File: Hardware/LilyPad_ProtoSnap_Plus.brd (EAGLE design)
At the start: 109.2 x 82.5 mm, 197 parts, among them J1 SEWTAP_LONG-2SIDE, J10 SEWTAP_LONG-2SIDE, J11 SEWTAP_LONG-2SIDE, J12 SEWTAP_LONG-2SIDE, J13 SEWTAP_LONG-2SIDE, J14 SEWTAP_LONG-2SIDE, J15 AMP FCI 10103594-0001LF, J2 SEWTAP_LONG-2SIDE, J3 SEWTAP_LONG-2SIDE, J4 SEWTAP_LONG-2SIDE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

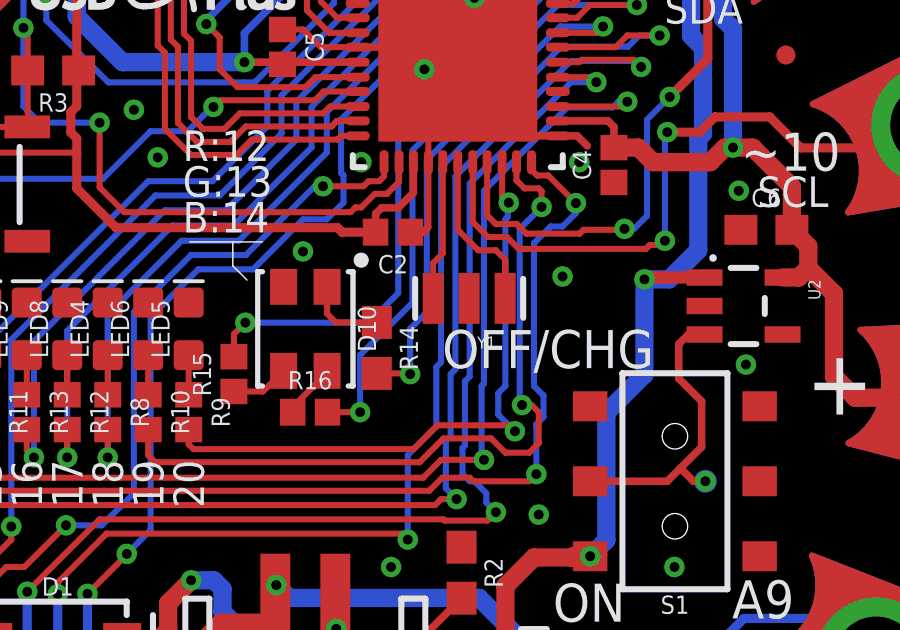
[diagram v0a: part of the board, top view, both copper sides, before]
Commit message: Added changes from reds review
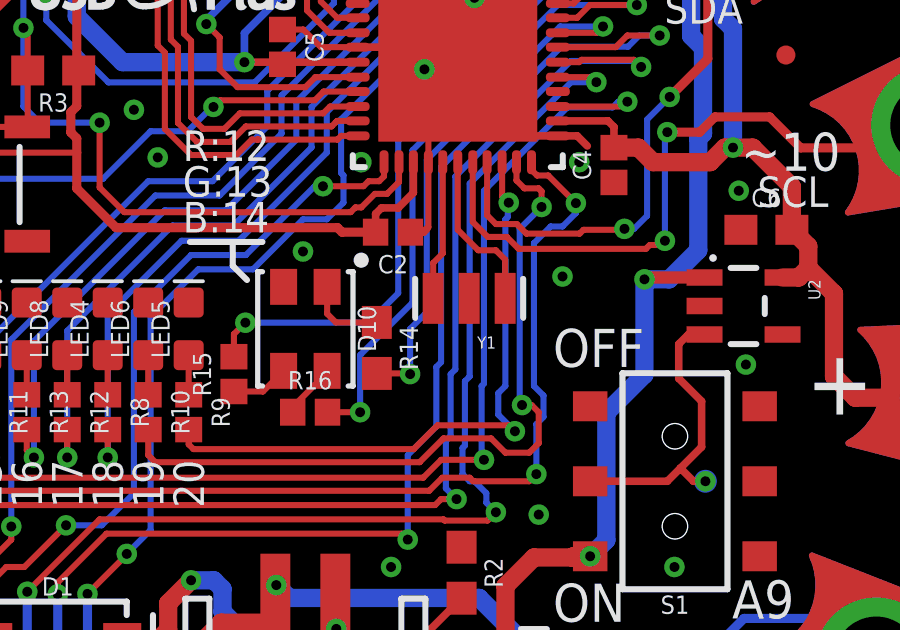
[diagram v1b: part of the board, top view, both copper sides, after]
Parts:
- R17: value 10k -> 1k
- R6: value 330 -> 2.2k
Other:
- board text added: "OFF"
- board text removed: "OFF/CHG"

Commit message: Ran engineering checklist
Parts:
- moved U$43 0.32 mm to (-21.1, 22.5)
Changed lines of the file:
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@@
 <layer number="22" name="bPlace" color="14" fill="1" visible="yes" active="yes"/>
 <layer number="23" name="tOrigins" color="15" fill="1" visible="no" active="yes"/>
-<layer number="24" name="bOrigins" color="15" fill="1" visible="no" active="yes"/>
+<layer number="24" name="bOrigins" color="15" fill="1" visible="yes" active="yes"/>
 <layer number="25" name="tNames" color="7" fill="1" visible="no" active="yes"/>
 <layer number="26" name="bNames" color="7" fill="1" visible="no" active="yes"/>
@@
 <layer number="28" name="bValues" color="7" fill="1" visible="no" active="yes"/>
 <layer number="29" name="tStop" color="7" fill="3" visible="no" active="yes"/>
-<layer number="30" name="bStop" color="7" fill="6" visible="yes" active="yes"/>
+<layer number="30" name="bStop" color="7" fill="6" visible="no" active="yes"/>
 <layer number="31" name="tCream" color="7" fill="4" visible="no" active="yes"/>
 <layer number="32" name="bCream" color="7" fill="5" visible="no" active="yes"/>
@@
 <element name="U$5" library="newLilypadParts" package="LILYPAD-WEARABLES_LOGO-LILYPAD" value="LILYLOGO_SHORT" x="-42.2671875" y="13.97" rot="MR90"/>
 <element name="U$6" library="newLilypadParts" package="LILYPAD-WEARABLES_LOGO-LILYPAD" value="LILYLOGO_SHORT" x="-42.2671875" y="-11.43" rot="MR90"/>
-<element name="U$43" library="newLilypadParts" package="LILYPAD-WEARABLES_LOGO-LILYPAD" value="LILYLOGO_SHORT" x="-21.082" y="22.86"/>
+<element name="U$43" library="newLilypadParts" package="LILYPAD-WEARABLES_LOGO-LILYPAD" value="LILYLOGO_SHORT" x="-21.082" y="22.5425"/>
 </elements>
 <signals>
@@
 <wire x1="1.7435" y1="8.389996875" x2="0.333440625" y2="8.389996875" width="0.2032" layer="1"/>
 <wire x1="0.333440625" y1="8.389996875" x2="0.3334375" y2="8.39" width="0.2032" layer="1"/>
-<wire x1="3.937" y1="19.2801875" x2="3.936996875" y2="19.240503125" width="0" layer="19" extent="1-1"/>
+<wire x1="3.936996875" y1="19.240503125" x2="3.937" y2="19.240503125" width="0.4064" layer="1"/>
+<wire x1="3.937" y1="19.240503125" x2="3.937" y2="19.2801875" width="0.4064" layer="1"/>
 </signal>
 <signal name="N$8">

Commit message: Updated reds QC check
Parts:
- D10: device newLilypadParts:PLCC4SMDLED -> SparkFun-LED:PLCC4SMDLED
- U5: value ATMEGA32U4_NOARDQFN3 -> 32U4; device newLilypadParts:QFN-44-PAD_1:1-LESS_PASTE -> SparkFun-IC-Microcontroller:QFN-44-PAD_1:1-LESS_PASTE
- moved C6 76.4 mm to (71.2, 55.4)
- moved J1 76.4 mm to (46.9, 72.2)
- moved J2 76.4 mm to (39.5, 66.8)
- moved JP3 76.4 mm to (71.9, 61.2)
- moved LOGO2 76.4 mm to (32.6, 76.2)
- moved LOGO4 76.4 mm to (8.26, 66.0)
- moved R1 76.4 mm to (62.5, 38.2)
- moved S3 76.4 mm to (97.8, 13.3)
- moved SLIDEOFF 76.4 mm to (97.8, 8.13)
- moved SLIDEON 76.4 mm to (97.8, 18.5)
- moved ST1 76.4 mm to (6.35, 66.0)
- moved TP1 76.4 mm to (49.5, 66.0)
- moved TP3 76.4 mm to (52.1, 66.0)
- moved TP4 76.4 mm to (54.6, 66.0)
- moved U$26 76.4 mm to (39.5, 66.8)
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
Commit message: Removed d2 90
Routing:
- net D2: track 114.5 -> 111.8 mm
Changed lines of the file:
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@@
 <grid distance="0.05" unitdist="inch" unit="inch" style="lines" multiple="1" display="yes" altdistance="0.0015625" altunitdist="inch" altunit="inch"/>
 <layers>
-<layer number="1" name="Top" color="4" fill="1" visible="yes" active="yes"/>
+<layer number="1" name="Top" color="4" fill="1" visible="no" active="yes"/>
 <layer number="2" name="Route2" color="1" fill="3" visible="no" active="no"/>
 <layer number="15" name="Route15" color="4" fill="6" visible="no" active="no"/>
@@
 <wire x1="66.119375" y1="59.451875" x2="64.61125" y2="59.451875" width="0.2032" layer="16"/>
 <wire x1="64.61125" y1="59.451875" x2="61.833125" y2="56.67375" width="0.2032" layer="16"/>
-<wire x1="41.91" y1="64.25533125" x2="41.91" y2="53.34" width="0.3048" layer="16"/>
-<wire x1="41.91" y1="53.34" x2="40.64" y2="52.07" width="0.3048" layer="16"/>
-<wire x1="40.64" y1="52.07" x2="40.64" y2="48.26" width="0.3048" layer="16"/>
-<wire x1="40.64" y1="48.26" x2="43.5371875" y2="48.26" width="0.3048" layer="16"/>
-<wire x1="43.5371875" y1="48.26" x2="43.815" y2="47.9821875" width="0.3048" layer="16"/>
+<wire x1="41.91" y1="64.25533125" x2="41.91" y2="49.8871875" width="0.3048" layer="16"/>
+<wire x1="41.91" y1="49.8871875" x2="43.815" y2="47.9821875" width="0.3048" layer="16"/>
 <via x="43.815" y="47.9821875" extent="1-16" drill="0.3302"/>
 <wire x1="44.6484375" y1="47.1090625" x2="59.8090625" y2="47.1090625" width="0.2032" layer="1"/>
